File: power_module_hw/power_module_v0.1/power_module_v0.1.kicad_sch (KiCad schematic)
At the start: 48 parts, among them Q1 BSS138, U3 INA226, U4 LDK130-ADJ_DFN6

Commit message: update the design
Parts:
- removed C11 (x2): 0.1uF, Capacitor_SMD:C_0603_1608Metric, symbol Device:C
- removed C11 (x2): 0.1uF, Capacitor_SMD:C_1206_3216Metric, symbol Device:C
- added C11: 0.1uF, Capacitor_SMD:C_0603_1608Metric, symbol Device:C
- added C11: 22uF, Capacitor_SMD:C_0603_1608Metric, symbol Device:C
- added C11: 0.1uF, Resistor_SMD:R_0402_1005Metric, symbol Device:C
- C11: value 0.1uF -> 47uF
- C11: value 0.1uF -> 1uF
- C11: value 0.1uF -> 47uF; footprint Capacitor_SMD:C_0603_1608Metric -> Capacitor_SMD:C_1210_3225Metric
- C11: value 0.1uF -> 22uF
- C11: footprint Capacitor_SMD:C_0603_1608Metric -> Capacitor_SMD:C_0402_1005Metric
- C11: value 0.1uF -> 100pF
- C11: value 0.1uF -> 10pF
- R6: value 1M -> 10K
- R6: value 1M -> 4.7K
- R6: value 1M -> 0R
- R6: value 1M -> 2.32K
- R6: value 1M -> 2.87K
- R6: value 1M -> 31.2K 1%
- R6: value 1M -> 1K
- R6: value 1M -> NC
- R6: value 1M -> 10K 1%
- R9: value R_Shunt_US -> 20mR
- U1: value ~ -> GD32E230F4V6TR
- U2: value ~ -> SiC45X
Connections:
- net GNDD is gone; now on net GNDA: C11.1, R6.1, R6.1, U1.12 (VSS), U3.2 (A0)
- net I2IC0_SDA is gone; now on net I2C0_SDA: R6.1, U3.4 (SDA)
- net +3.3V: now also C11.1
- net +5VA: now also C11.1, C11.1
- net GNDA: now also C11.2, C11.2, C11.2
- net GPIO2: now also U1.7 (PA4); no longer U1.11 (PB1)
- net PWR_ALERT: now also U1.19 (OSCIN); no longer U1.7 (PA4)
- net UART_RXD: now also U1.6 (PA3); no longer U1.5 (PA2)
- net UART_TXD: now also U1.5 (PA2); no longer U1.4 (PA1)
- net ~{PWR_EN}: now also U1.11 (PB1); no longer U1.8 (PA5)
- net ~{SENSOR_ALERT}: now also U1.10 (PA7); no longer U1.6 (PA3)
- net GPIO0 renamed SWDIO
- net GPIO1 renamed SWCLK
- new net GPIO3: U1.8 (PA5)
- no-connect marks 11 -> 10
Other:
- note added: "ADDR = 0x40"
- note added: "ADDR = 0x5E"
- note added: "Vout = 0.8*(1+R12/R13)"
- moved on the sheet: C11, R6

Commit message: update the design and ship out for mfg
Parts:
- C11: footprint Resistor_SMD:R_0402_1005Metric -> Capacitor_SMD:C_0402_1005Metric
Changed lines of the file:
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@@
       (effects (font (size 1.27 1.27)) (justify right))
     )
-    (property "Footprint" "Resistor_SMD:R_0402_1005Metric" (at 78.4352 150.495 0)
+    (property "Footprint" "Capacitor_SMD:C_0402_1005Metric" (at 78.4352 150.495 0)
       (effects (font (size 1.27 1.27)) hide)
     )

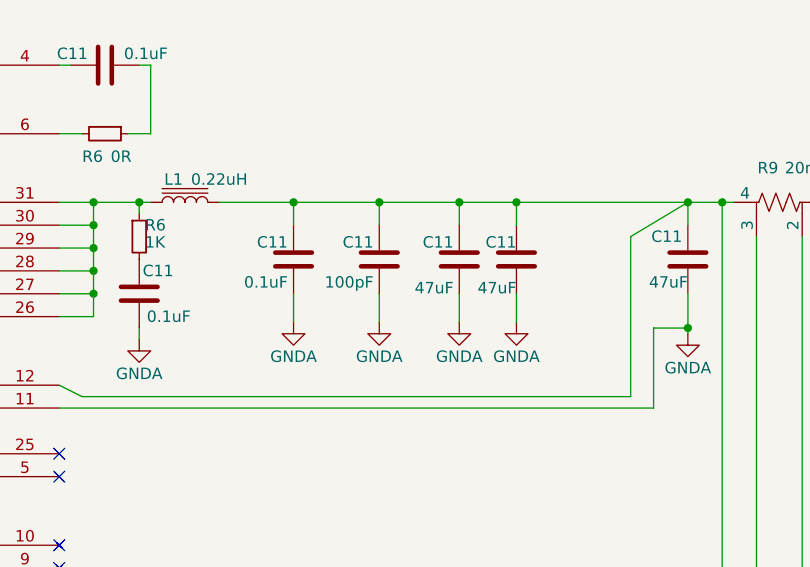
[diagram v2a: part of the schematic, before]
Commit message: update the bom
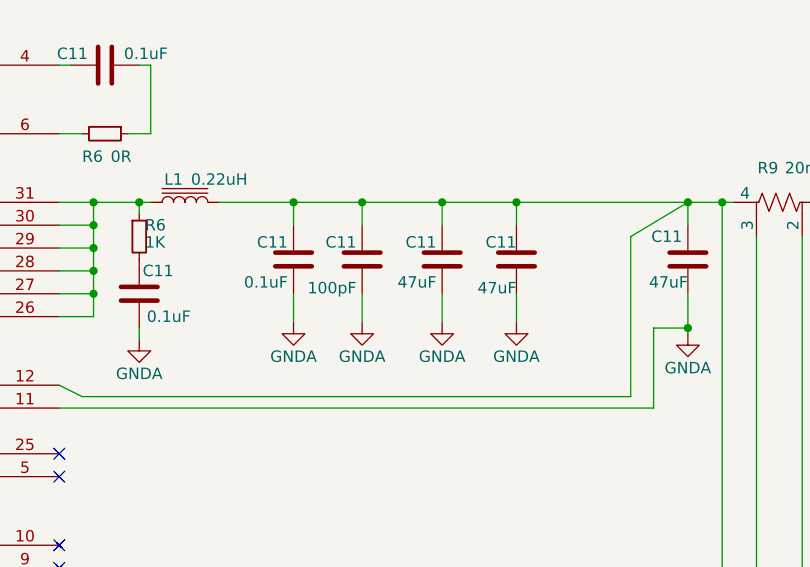
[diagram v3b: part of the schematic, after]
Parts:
- C11: value 47uF -> 100pF
- C11: value 100pF -> 47uF
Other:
- moved on the sheet: C11
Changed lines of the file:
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@@
   (junction (at 281.94 107.95) (diameter 0) (color 0 0 0 0)
   )
-  (junction (at 322.58 100.33) (diameter 0) (color 0 0 0 0)
-  )
   (junction (at 120.65 143.51) (diameter 0) (color 0 0 0 0)
   )
@@
   (junction (at 110.49 146.05) (diameter 0) (color 0 0 0 0)
   )
+  (junction (at 320.675 100.33) (diameter 0) (color 0 0 0 0)
+  )
   (junction (at 77.47 138.43) (diameter 0) (color 0 0 0 0)
   )
+  (junction (at 311.785 100.33) (diameter 0) (color 0 0 0 0)
+  )
   (junction (at 242.57 140.97) (diameter 0) (color 0 0 0 0)
   )
@@
   (junction (at 287.02 100.33) (diameter 0) (color 0 0 0 0)
   )
-  (junction (at 313.69 100.33) (diameter 0) (color 0 0 0 0)
-  )
   (junction (at 304.165 100.33) (diameter 0) (color 0 0 0 0)
   )
@@
     (stroke (width 0) (type default))
   )
-  (wire (pts (xy 322.58 100.33) (xy 322.58 102.87))
+  (wire (pts (xy 311.785 100.33) (xy 311.785 102.87))
     (stroke (width 0) (type default))
   )
@@
     (stroke (width 0) (type default))
   )
-  (wire (pts (xy 313.69 100.33) (xy 313.69 102.87))
+  (wire (pts (xy 320.675 100.33) (xy 320.675 102.87))
     (stroke (width 0) (type default))
   )
@@
     (stroke (width 0) (type default))
   )
+  (wire (pts (xy 320.675 100.33) (xy 328.93 100.33))
+    (stroke (width 0) (type default))
+  )
   (wire (pts (xy 351.79 100.33) (xy 353.06 100.33))
     (stroke (width 0) (type default))
@@
     (stroke (width 0) (type default))
   )
-  (wire (pts (xy 313.69 110.49) (xy 313.69 113.665))
+  (wire (pts (xy 320.675 110.49) (xy 320.675 113.665))
     (stroke (width 0) (type default))
   )
@@
     (stroke (width 0) (type default))
   )
-  (wire (pts (xy 322.58 113.665) (xy 322.58 110.49))
+  (wire (pts (xy 311.785 110.49) (xy 311.785 113.665))
     (stroke (width 0) (type default))
   )
@@
     (stroke (width 0) (type default))
   )
-  (wire (pts (xy 322.58 100.33) (xy 328.93 100.33))
-    (stroke (width 0) (type default))
-  )
   (wire (pts (xy 344.17 114.3) (xy 347.98 114.3))
     (stroke (width 0) (type default))
@@
     (stroke (width 0) (type default))
   )
+  (wire (pts (xy 311.785 100.33) (xy 320.675 100.33))
+    (stroke (width 0) (type default))
+  )
   (wire (pts (xy 271.78 190.5) (xy 355.6 190.5))
     (stroke (width 0) (type default))
@@
     (stroke (width 0) (type default))
   )
-  (wire (pts (xy 313.69 100.33) (xy 322.58 100.33))
-    (stroke (width 0) (type default))
-  )
   (wire (pts (xy 120.65 96.52) (xy 127 96.52))
     (stroke (width 0) (type default))
@@
     (stroke (width 0) (type default))
   )
-  (wire (pts (xy 304.165 100.33) (xy 313.69 100.33))
+  (wire (pts (xy 304.165 100.33) (xy 311.785 100.33))
     (stroke (width 0) (type default))
   )
@@
     )
   )
-  (symbol (lib_id "power:GNDA") (at 322.58 113.665 0) (unit 1)
+  (symbol (lib_id "power:GNDA") (at 320.675 113.665 0) (unit 1)
     (in_bom yes) (on_board yes) (dnp no)
-    (property "Reference" "#PWR023" (at 322.58 120.015 0)
+    (property "Reference" "#PWR023" (at 320.675 120.015 0)
       (effects (font (size 1.27 1.27)) hide)
     )
-    (property "Value" "GNDA" (at 322.58 117.475 0)
+    (property "Value" "GNDA" (at 320.675 117.475 0)
       (effects (font (size 1.27 1.27)))
     )
-    (property "Footprint" "" (at 322.58 113.665 0)
+    (property "Footprint" "" (at 320.675 113.665 0)
       (effects (font (size 1.27 1.27)) hide)
     )
-    (property "Datasheet" "" (at 322.58 113.665 0)
+    (property "Datasheet" "" (at 320.675 113.665 0)
       (effects (font (size 1.27 1.27)) hide)
     )
@@
     )
   )
-  (symbol (lib_id "Device:C") (at 322.58 106.68 0) (unit 1)
+  (symbol (lib_id "Device:C") (at 311.785 106.68 0) (unit 1)
     (in_bom yes) (on_board yes) (dnp no)
-    (property "Reference" "C11" (at 321.945 104.775 0)
+    (property "Reference" "C11" (at 311.15 104.775 0)
       (effects (font (size 1.27 1.27)) (justify right))
     )
-    (property "Value" "47uF" (at 321.945 109.855 0)
+    (property "Value" "100pF" (at 311.15 109.855 0)
       (effects (font (size 1.27 1.27)) (justify right))
     )
-    (property "Footprint" "Capacitor_SMD:C_0603_1608Metric" (at 323.5452 110.49 0)
+    (property "Footprint" "Capacitor_SMD:C_0603_1608Metric" (at 312.7502 110.49 0)
       (effects (font (size 1.27 1.27)) hide)
     )
-    (property "Datasheet" "~" (at 322.58 106.68 0)
+    (property "Datasheet" "~" (at 311.785 106.68 0)
       (effects (font (size 1.27 1.27)) hide)
     )
@@
     )
   )
-  (symbol (lib_id "Device:C") (at 313.69 106.68 0) (unit 1)
+  (symbol (lib_id "Device:C") (at 320.675 106.68 0) (unit 1)
     (in_bom yes) (on_board yes) (dnp no)
-    (property "Reference" "C11" (at 313.055 104.775 0)
+    (property "Reference" "C11" (at 320.04 104.775 0)
       (effects (font (size 1.27 1.27)) (justify right))
     )
-    (property "Value" "100pF" (at 313.055 109.22 0)
+    (property "Value" "47uF" (at 320.04 109.22 0)
       (effects (font (size 1.27 1.27)) (justify right))
     )
-    (property "Footprint" "Capacitor_SMD:C_1206_3216Metric" (at 314.6552 110.49 0)
+    (property "Footprint" "Capacitor_SMD:C_1206_3216Metric" (at 321.6402 110.49 0)
       (effects (font (size 1.27 1.27)) hide)
     )
-    (property "Datasheet" "~" (at 313.69 106.68 0)
+    (property "Datasheet" "~" (at 320.675 106.68 0)
       (effects (font (size 1.27 1.27)) hide)
     )
@@
     )
   )
-  (symbol (lib_id "power:GNDA") (at 313.69 113.665 0) (unit 1)
+  (symbol (lib_id "power:GNDA") (at 311.785 113.665 0) (unit 1)
     (in_bom yes) (on_board yes) (dnp no)
-    (property "Reference" "#PWR020" (at 313.69 120.015 0)
+    (property "Reference" "#PWR020" (at 311.785 120.015 0)
       (effects (font (size 1.27 1.27)) hide)
     )
-    (property "Value" "GNDA" (at 313.69 117.475 0)
+    (property "Value" "GNDA" (at 311.785 117.475 0)
       (effects (font (size 1.27 1.27)))
     )
-    (property "Footprint" "" (at 313.69 113.665 0)
+    (property "Footprint" "" (at 311.785 113.665 0)
       (effects (font (size 1.27 1.27)) hide)
     )
-    (property "Datasheet" "" (at 313.69 113.665 0)
+    (property "Datasheet" "" (at 311.785 113.665 0)
       (effects (font (size 1.27 1.27)) hide)
     )
